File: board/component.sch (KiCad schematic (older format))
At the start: 3 parts, among them P601 Y, P602 Pb, P603 Pr

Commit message: More footprints
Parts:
- removed P601: Y, symbol BNC
- removed P602: Pb, symbol BNC
- removed P603: Pr, symbol BNC
- added P601: 3-RCA, symbol 3-RCA
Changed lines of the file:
@@
 LIBS:testpoint
 LIBS:ad9984-power
+LIBS:3-rca
 EELAYER 25 0
 EELAYER END
@@
 Sheet 6 6
 Title "TOFE VGA - Component"
-Date "2015-11-25"
+Date "2016-01-15"
 Rev "1.0"
 Comp "Kenny Duffus <kenny@duffus.org>"
@@
 Comment4 ""
 $EndDescr
-$Comp
-L BNC P601
-U 1 1 5655ABB5
-P 5200 3000
-F 0 "P601" H 5210 3120 50  0000 C CNN
-F 1 "Y" V 5310 2940 50  0000 C CNN
-F 2 "" H 5200 3000 60  0001 C CNN
-F 3 "" H 5200 3000 60  0000 C CNN
-	1    5200 3000
-	-1   0    0    -1
-$EndComp
-$Comp
-L BNC P602
-U 1 1 5655ABED
-P 5200 3450
-F 0 "P602" H 5210 3570 50  0000 C CNN
-F 1 "Pb" V 5310 3390 50  0000 C CNN
-F 2 "" H 5200 3450 60  0001 C CNN
-F 3 "" H 5200 3450 60  0000 C CNN
-	1    5200 3450
-	-1   0    0    -1
-$EndComp
-$Comp
-L BNC P603
-U 1 1 5655AC38
-P 5200 3900
-F 0 "P603" H 5210 4020 50  0000 C CNN
-F 1 "Pr" V 5310 3840 50  0000 C CNN
-F 2 "" H 5200 3900 60  0001 C CNN
-F 3 "" H 5200 3900 60  0000 C CNN
-	1    5200 3900
-	-1   0    0    -1
-$EndComp
 Text HLabel 5450 3000 2    60   Input ~ 0
 COMP_Y
-Text HLabel 5450 3450 2    60   Input ~ 0
+Text HLabel 5450 3350 2    60   Input ~ 0
 COMP_Pb
-Text HLabel 5450 3900 2    60   Input ~ 0
+Text HLabel 5450 3700 2    60   Input ~ 0
 COMP_Pr
 $Comp
 L GND #PWR051
 U 1 1 5655AC8B
-P 5000 4200
-F 0 "#PWR051" H 5000 3950 50  0001 C CNN
-F 1 "GND" H 5000 4050 50  0000 C CNN
-F 2 "" H 5000 4200 60  0000 C CNN
-F 3 "" H 5000 4200 60  0000 C CNN
-	1    5000 4200
+P 5000 4000
+F 0 "#PWR051" H 5000 3750 50  0001 C CNN
+F 1 "GND" H 5000 3850 50  0000 C CNN
+F 2 "" H 5000 4000 60  0000 C CNN
+F 3 "" H 5000 4000 60  0000 C CNN
+	1    5000 4000
 	1    0    0    -1
 $EndComp
 Wire Wire Line
-	5000 4100 5200 4100
-Wire Wire Line
-	5000 3200 5000 4200
-Wire Wire Line
-	5200 3650 5000 3650
-Connection ~ 5000 4100
-Wire Wire Line
 	5200 3200 5000 3200
-Connection ~ 5000 3650
 Wire Wire Line
 	5350 3000 5450 3000
 Wire Wire Line
-	5350 3450 5450 3450
+	5350 3350 5450 3350
 Wire Wire Line
-	5350 3900 5450 3900
+	5350 3700 5450 3700
+$Comp
+L 3-RCA P601
+U 1 1 5698F0C6
+P 5200 3350
+F 0 "P601" H 5200 3900 50  0000 C CNN
+F 1 "3-RCA" V 5400 3300 50  0001 C CNN
+F 2 "" H 5200 3000 50  0001 C CNN
+F 3 "" H 5200 3000 50  0000 C CNN
+	1    5200 3350
+	-1   0    0    -1
+$EndComp
+Wire Wire Line
+	5200 3900 5000 3900
+Wire Wire Line
+	5000 3200 5000 4000
+Wire Wire Line
+	5200 3550 5000 3550
+Connection ~ 5000 3900
+Connection ~ 5000 3550
 $EndSCHEMATC

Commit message: Finish footprint assignment
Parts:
- P601: footprint (none) -> 3-RCA:MR-100H
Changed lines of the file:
@@
 F 0 "P601" H 5200 3900 50  0000 C CNN
 F 1 "3-RCA" V 5400 3300 50  0001 C CNN
-F 2 "" H 5200 3000 50  0001 C CNN
+F 2 "3-RCA:MR-100H" H 5200 3000 50  0001 C CNN
 F 3 "" H 5200 3000 50  0000 C CNN
 	1    5200 3350

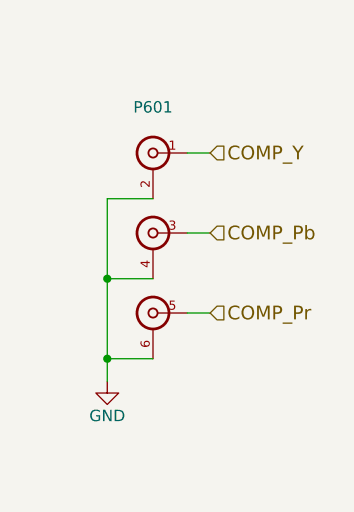
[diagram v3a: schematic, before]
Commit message: Adding an analog ground.
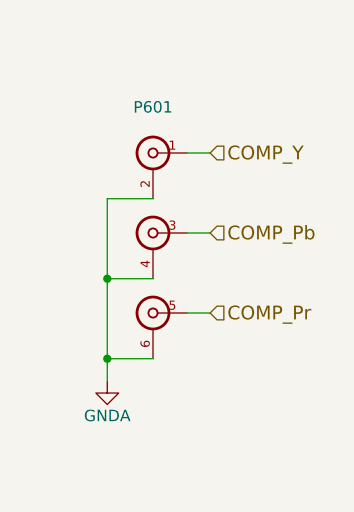
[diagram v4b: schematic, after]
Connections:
- net GND renamed GNDA
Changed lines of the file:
@@
 COMP_Pr
 $Comp
-L GND #PWR051
+L GNDA #PWR051
 U 1 1 5655AC8B
 P 5000 4000
 F 0 "#PWR051" H 5000 3750 50  0001 C CNN
-F 1 "GND" H 5000 3850 50  0000 C CNN
+F 1 "GNDA" H 5000 3850 50  0000 C CNN
 F 2 "" H 5000 4000 60  0000 C CNN
 F 3 "" H 5000 4000 60  0000 C CNN
